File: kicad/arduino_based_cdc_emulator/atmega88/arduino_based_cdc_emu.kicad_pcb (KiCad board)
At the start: 2 copper layers, 13 parts, among them IC1 ATMEGA88-A, P1 CONN_5, P2 CONN_2, U1 78L05, X1 20MHz

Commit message: same changes
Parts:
- added P3: CONN_3, Pin_Headers:Pin_Header_Straight_1x01, F.Cu at (104.6, 107.1)
- P1: value CONN_5 -> CONN_1
- P2: footprint Pin_Headers:Pin_Header_Straight_1x02 -> Pin_Headers:Pin_Header_Straight_1x05
- moved P1 39.5 mm to (101.4, 117.1)
- moved C2 25.0 mm to (116.8, 107.0), turned to 180 degrees
- moved C1 24.1 mm to (101.9, 104.5), turned to 270 degrees
- moved X1 23.2 mm to (111.5, 103.2)
- moved C3 21.6 mm to (114.2, 119.6), turned to 90 degrees
- moved P2 17.5 mm to (124.1, 114.2), turned to 180 degrees
- moved IC1 15.6 mm to (109.5, 112.0)
- moved R4 14.1 mm to (121.5, 105.1), turned to 90 degrees
- moved R1 14.0 mm to (104.4, 119.3), turned to 90 degrees
- moved R3 13.4 mm to (119.3, 112.6), turned to 0 degrees
- moved C4 10.3 mm to (119.3, 114.9), turned to 180 degrees
- moved U1 9.58 mm to (120.8, 120.0), turned to 270 degrees
- moved R2 7.68 mm to (109.5, 120.5), turned to 180 degrees
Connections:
- IC1 pad 16: (no net) -> /MISO
- IC1 pad 19: Net-(C1-Pad2) -> (no net)
- IC1 pad 22: Net-(C2-Pad2) -> (no net)
- IC1 pad 29: Net-(IC1-Pad29) -> /RESET
- IC1 pad 7: (no net) -> Net-(C2-Pad2)
- IC1 pad 8: (no net) -> Net-(C1-Pad2)
- P2 pad 1: RX -> +5V
- P2 pad 2: TX -> /RESET
- R3 pad 1: Net-(IC1-Pad29) -> /RESET
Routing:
- net GND: track 46.7 -> 106.8 mm
- net /DataIn: track 34.0 -> 4.40 mm
- net +5V: track 65.6 -> 40.8 mm
- net /DataOut: track 12.7 -> 34.1 mm
- net /Clock: track 26.3 -> 7.78 mm
- net Net-(IC1-Pad15): track 3.04 -> 17.2 mm
- net /RESET: track 0.00 -> 11.9 mm
- net /MISO: track 0.00 -> 9.94 mm
- net +12V: track 10.8 -> 20.1 mm
- net Net-(IC1-Pad29): track 8.33 -> 0.00 mm
- net Net-(C2-Pad2): track 23.4 -> 17.5 mm
- net Net-(C1-Pad2): track 10.2 -> 14.8 mm
- net Net-(IC1-Pad32): track 5.63 -> 8.87 mm
- net RX: track 12.2 -> 10.5 mm
- net TX: track 12.7 -> 11.5 mm
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- removed copper zone on F.Cu, net GND
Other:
- board outline added: 26.6 x 23.5 mm

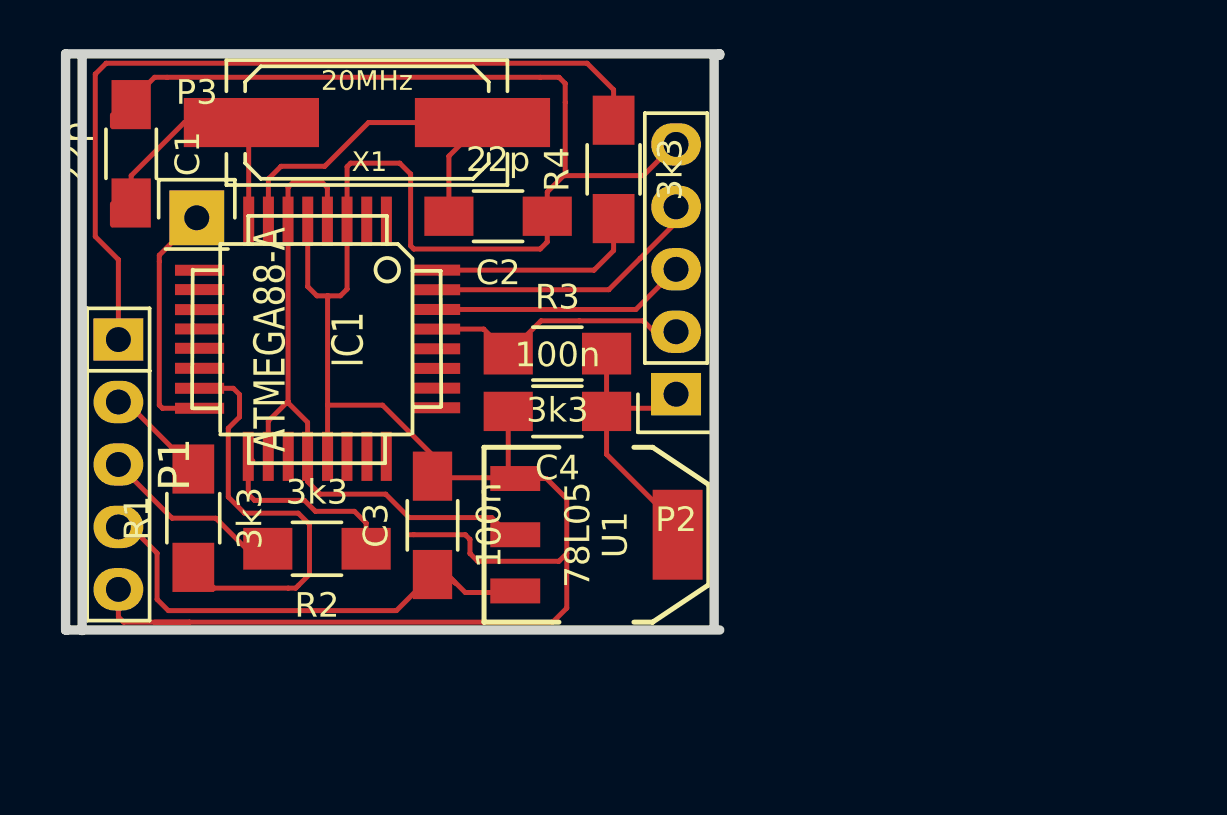
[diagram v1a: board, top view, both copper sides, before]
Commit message: pcb, really need rework.
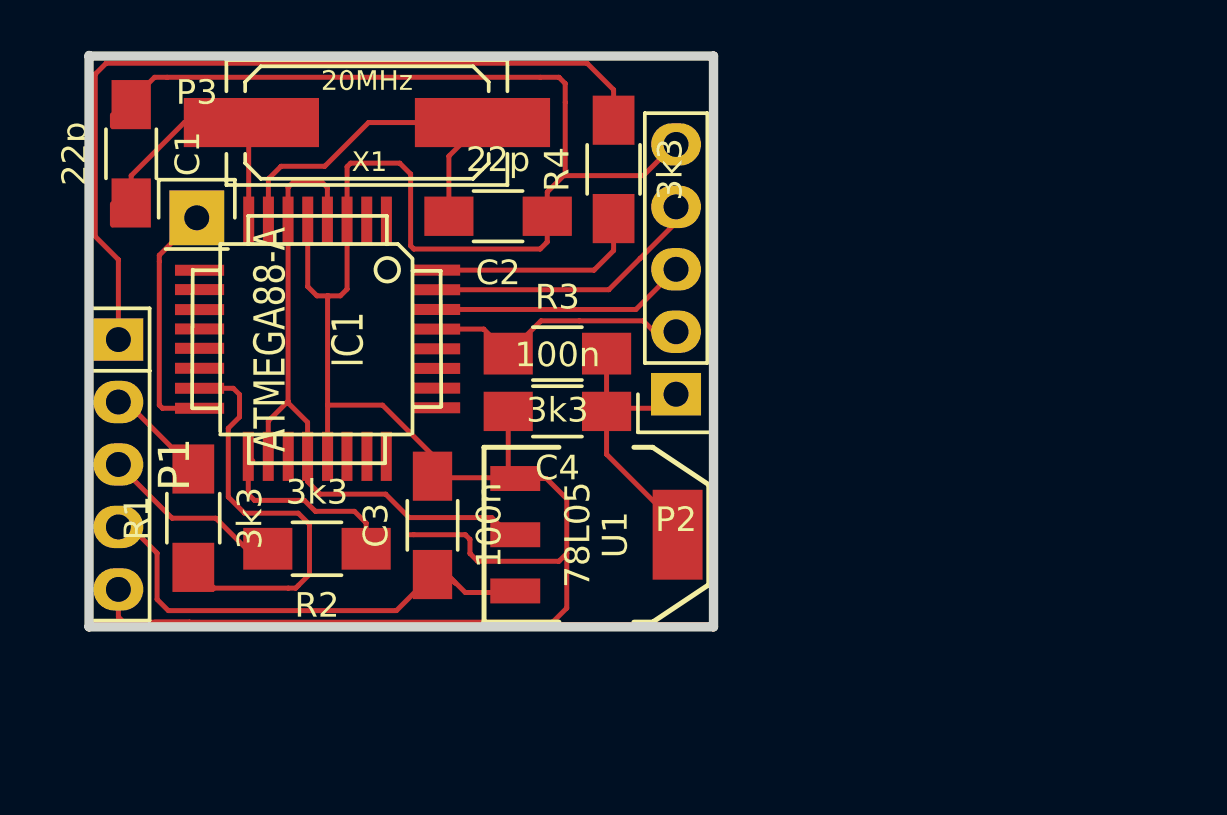
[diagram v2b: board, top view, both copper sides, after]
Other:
- board size 26.6 x 23.5 mm -> 25.4 x 23.2 mm
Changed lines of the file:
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@@
-(kicad_pcb (version 4) (host pcbnew 0.201505041002+5641~23~ubuntu14.04.1-product)
+(kicad_pcb (version 4) (host pcbnew 0.201511171411+6319~30~ubuntu14.04.1-product)
   (general
     (links 34)
     (no_connects 1)
-    (area 96.636115 92.566902 136.873055 124.333001)
+    (area 98.4385 95.5548 137.922002 124.015501)
     (thickness 1.6002)
-    (drawings 8)
+    (drawings 6)
     (tracks 187)
     (zones 0)
@@
     )
   )
-  (gr_line (start 125.6284 123.7996) (end 125.6284 100.4316) (angle 90) (layer Edge.Cuts) (width 0.381))
-  (gr_line (start 99.9236 100.4316) (end 99.9744 100.4316) (angle 90) (layer Edge.Cuts) (width 0.381))
-  (gr_line (start 99.9236 123.8504) (end 99.9236 100.4316) (angle 90) (layer Edge.Cuts) (width 0.381))
-  (gr_line (start 99.2505 123.825) (end 99.314 123.825) (angle 90) (layer Edge.Cuts) (width 0.381))
-  (gr_line (start 99.2505 100.3935) (end 99.2505 123.825) (angle 90) (layer Edge.Cuts) (width 0.381))
-  (gr_line (start 99.2505 123.825) (end 125.857 123.825) (angle 90) (layer Edge.Cuts) (width 0.381))
-  (gr_line (start 125.857 100.3935) (end 125.857 100.457) (angle 90) (layer Edge.Cuts) (width 0.381))
-  (gr_line (start 99.2505 100.3935) (end 125.857 100.3935) (angle 90) (layer Edge.Cuts) (width 0.381))
+  (gr_line (start 125.603 123.698) (end 125.603 100.4824) (angle 90) (layer Edge.Cuts) (width 0.381))
+  (gr_line (start 100.203 123.698) (end 125.603 123.698) (angle 90) (layer Edge.Cuts) (width 0.381))
+  (gr_line (start 100.203 100.4824) (end 125.603 100.4824) (angle 90) (layer Edge.Cuts) (width 0.381))
+  (dimension 25.4 (width 0.3048) (layer Dwgs.User)
+    (gr_text "25.400 mm" (at 112.903 97.4344) (layer Dwgs.User)
+      (effects (font (size 2.032 1.524) (thickness 0.3048)))
+    )
+    (feature1 (pts (xy 125.603 100.457) (xy 125.603 95.8088)))
+    (feature2 (pts (xy 100.203 100.457) (xy 100.203 95.8088)))
+    (crossbar (pts (xy 100.203 99.06) (xy 125.603 99.06)))
+    (arrow1a (pts (xy 125.603 99.06) (xy 124.476496 99.646421)))
+    (arrow1b (pts (xy 125.603 99.06) (xy 124.476496 98.473579)))
+    (arrow2a (pts (xy 100.203 99.06) (xy 101.329504 99.646421)))
+    (arrow2b (pts (xy 100.203 99.06) (xy 101.329504 98.473579)))
+  )
+  (gr_line (start 100.203 100.457) (end 100.203 123.698) (angle 90) (layer Edge.Cuts) (width 0.381))
+  (dimension 23.495 (width 0.3048) (layer Dwgs.User)
+    (gr_text "23.495 mm" (at 131.1656 112.0775 270) (layer Dwgs.User)
+      (effects (font (size 2.032 1.524) (thickness 0.3048)))
+    )
+    (feature1 (pts (xy 125.603 123.825) (xy 132.7912 123.825)))
+    (feature2 (pts (xy 125.603 100.33) (xy 132.7912 100.33)))
+    (crossbar (pts (xy 129.54 100.33) (xy 129.54 123.825)))
+    (arrow1a (pts (xy 129.54 123.825) (xy 128.953579 122.698496)))
+    (arrow1b (pts (xy 129.54 123.825) (xy 130.126421 122.698496)))
+    (arrow2a (pts (xy 129.54 100.33) (xy 128.953579 101.456504)))
+    (arrow2b (pts (xy 129.54 100.33) (xy 130.126421 101.456504)))
+  )
   (segment (start 108.29798 107.19816) (end 108.29798 105.82402) (width 0.2032) (layer Front) (net 1))
   (segment (start 109.6645 105.6005) (end 109.89818 105.83418) (width 0.2032) (layer Front) (net 1))
@@
   (segment (start 123.444 118.872) (end 124.206 119.634) (width 0.2032) (layer Front) (net 1))
   (segment (start 121.253 116.681) (end 124.206 119.634) (width 0.2032) (layer Front) (net 1))
-  (segment (start 107.474 120.523) (end 106.6038 120.523) (width 0.2032) (layer Front) (net 2) (status C00000))
-  (segment (start 106.6038 120.523) (end 105.3592 119.2784) (width 0.2032) (layer Front) (net 2) (status 400000))
+  (segment (start 107.474 120.523) (end 106.6038 120.523) (width 0.2032) (layer Front) (net 2))
+  (segment (start 106.6038 120.523) (end 105.3592 119.2784) (width 0.2032) (layer Front) (net 2))
   (segment (start 105.3592 119.2784) (end 103.5812 119.2784) (width 0.2032) (layer Front) (net 2))
-  (segment (start 103.5812 119.2784) (end 101.3968 117.094) (width 0.2032) (layer Front) (net 2) (status 800000))
+  (segment (start 103.5812 119.2784) (end 101.3968 117.094) (width 0.2032) (layer Front) (net 2))
   (segment (start 106.712 120.8405) (end 106.712 120.555) (width 0.2032) (layer Front) (net 2))
-  (segment (start 101.3968 114.554) (end 101.7204 114.554) (width 0.2032) (layer Front) (net 3) (status C00000))
-  (segment (start 101.7204 114.554) (end 104.4448 117.2784) (width 0.2032) (layer Front) (net 3) (status C00000))
+  (segment (start 101.3968 114.554) (end 101.7204 114.554) (width 0.2032) (layer Front) (net 3))
+  (segment (start 101.7204 114.554) (end 104.4448 117.2784) (width 0.2032) (layer Front) (net 3))
   (segment (start 103.9495 116.8085) (end 103.9495 116.586) (width 0.2032) (layer Front) (net 3))
-  (segment (start 101.3968 112.014) (end 101.3968 108.7628) (width 0.2032) (layer Front) (net 4) (status 400000))
+  (segment (start 101.3968 112.014) (end 101.3968 108.7628) (width 0.2032) (layer Front) (net 4))
   (segment (start 101.3968 108.7628) (end 100.457 107.823) (width 0.2032) (layer Front) (net 4))
   (segment (start 100.457 101.219) (end 100.9015 100.7745) (width 0.2032) (layer Front) (net 4))
@@
   (segment (start 120.4595 100.7745) (end 100.9015 100.7745) (width 0.2032) (layer Front) (net 4))
   (segment (start 104.2924 123.5075) (end 101.6127 123.5075) (width 0.2032) (layer Front) (net 5))
-  (segment (start 101.3968 123.2916) (end 101.3968 122.174) (width 0.2032) (layer Front) (net 5) (status 800000))
+  (segment (start 101.3968 123.2916) (end 101.3968 122.174) (width 0.2032) (layer Front) (net 5))
   (segment (start 101.6127 123.5075) (end 101.3968 123.2916) (width 0.2032) (layer Front) (net 5))
   (segment (start 101.9175 102.4575) (end 101.9175 102.2985) (width 0.2032) (layer Front) (net 5))
@@
   (segment (start 113.697 103.156) (end 113.665 103.124) (width 0.2032) (layer Front) (net 7))
   (segment (start 115.602 103.664) (end 115.062 103.124) (width 0.2032) (layer Front) (net 7))
-  (segment (start 101.3968 119.634) (end 101.9048 119.634) (width 0.2032) (layer Front) (net 8) (status C00000))
-  (segment (start 101.9048 119.634) (end 102.9716 120.7008) (width 0.2032) (layer Front) (net 8) (status 400000))
+  (segment (start 101.3968 119.634) (end 101.9048 119.634) (width 0.2032) (layer Front) (net 8))
+  (segment (start 101.9048 119.634) (end 102.9716 120.7008) (width 0.2032) (layer Front) (net 8))
   (segment (start 102.9716 120.7008) (end 102.9716 122.5804) (width 0.2032) (layer Front) (net 8))
   (segment (start 102.9716 122.5804) (end 103.4288 123.0376) (width 0.2032) (layer Front) (net 8))
   (segment (start 103.4288 123.0376) (end 112.7059 123.0376) (width 0.2032) (layer Front) (net 8))
-  (segment (start 112.7059 123.0376) (end 114.173 121.5705) (width 0.2032) (layer Front) (net 8) (status 800000))
+  (segment (start 112.7059 123.0376) (end 114.173 121.5705) (width 0.2032) (layer Front) (net 8))
   (segment (start 114.808 121.634) (end 114.8395 121.634) (width 0.2032) (layer Front) (net 8))
   (segment (start 114.8395 121.634) (end 115.5065 122.301) (width 0.2032) (layer Front) (net 8))

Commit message: updates
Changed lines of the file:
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@@
-(kicad_pcb (version 4) (host pcbnew 0.201511171411+6319~30~ubuntu14.04.1-product)
+(kicad_pcb (version 20160815) (host pcbnew 4.1.0-alpha+201608211231+7083~46~ubuntu16.04.1-product)
   (general
     (links 34)
     (no_connects 1)
-    (area 98.4385 95.5548 137.922002 124.015501)
+    (area 99.797799 95.8088 137.922001 123.88946)
     (thickness 1.6002)
     (drawings 6)
@@
     (pad_to_mask_clearance 0.254)
     (aux_axis_origin 0 0)
-    (visible_elements FFFFFF7F)
+    (visible_elements FFFEFF7F)
     (pcbplotparams
       (layerselection 0x00030_80000001)
@@
       (hpglpenspeed 20)
       (hpglpendiameter 15)
-      (hpglpenoverlay 2)
       (psnegative false)
       (psa4output false)
@@
     (uvia_dia 0.508)
     (uvia_drill 0.127)
+    (diff_pair_gap 0.25)
+    (diff_pair_width 0.2)
     (add_net +12V)
     (add_net +5V)
@@
     (tags "capacitor 1206")
     (attr smd)
-    (fp_text reference C1 (at 0 -2.3 270) (layer F.SilkS)
-      (effects (font (size 1 1) (thickness 0.15)))
-    )
-    (fp_text value 22p (at 0 2.3 270) (layer F.SilkS)
+    (fp_text reference C1 (at 4.3925 -0.1325 270) (layer F.SilkS)
+      (effects (font (size 1 1) (thickness 0.15)))
+    )
+    (fp_text value 22p (at 4.7371 0.0508 270) (layer F.SilkS)
       (effects (font (size 1 1) (thickness 0.15)))
     )
@@
       (effects (font (size 1 1) (thickness 0.15)))
     )
-    (fp_text value 22p (at 0 2.3 180) (layer F.SilkS)
+    (fp_text value 22p (at -2.6543 -1.8034 180) (layer F.SilkS)
       (effects (font (size 1 1) (thickness 0.15)))
     )
@@
     (tags "capacitor 1206")
     (attr smd)
-    (fp_text reference C3 (at 0 -2.3 90) (layer F.SilkS)
-      (effects (font (size 1 1) (thickness 0.15)))
-    )
-    (fp_text value 100n (at 0 2.3 90) (layer F.SilkS)
+    (fp_text reference C3 (at 0.8205 -2.123 180) (layer F.SilkS)
+      (effects (font (size 1 1) (thickness 0.15)))
+    )
+    (fp_text value 100n (at 1.57734 1.55448 90) (layer F.SilkS)
       (effects (font (size 1 1) (thickness 0.15)))
     )
@@
     (tags "capacitor 1206")
     (attr smd)
-    (fp_text reference C4 (at 0 -2.3 180) (layer F.SilkS)
-      (effects (font (size 1 1) (thickness 0.15)))
-    )
-    (fp_text value 100n (at 0 2.3 180) (layer F.SilkS)
+    (fp_text reference C4 (at 0.003 4.185 360) (layer F.SilkS)
+      (effects (font (size 1 1) (thickness 0.15)))
+    )
+    (fp_text value 100n (at -1.47828 4.40436 180) (layer F.SilkS)
       (effects (font (size 1 1) (thickness 0.15)))
     )
@@
   (module SMD_Packages:TQFP-32 (layer Front)
     (at 109.474 112.014 270)
-    (fp_text reference IC1 (at 0 -1.27 270) (layer F.SilkS)
+    (fp_text reference IC1 (at 0.036 -2.126 270) (layer F.SilkS)
       (effects (font (size 1.27 1.016) (thickness 0.2032)))
     )
@@
     (descr "Through hole pin header")
     (tags "pin header")
-    (fp_text reference P1 (at 0 -2.286 270) (layer F.SilkS)
+    (fp_text reference P1 (at 0 -2.286 270) (layer F.SilkS) hide
       (effects (font (size 1.27 1.27) (thickness 0.2032)))
     )
@@
     (tags "resistor 1206")
     (attr smd)
-    (fp_text reference R1 (at 0 -2.3 90) (layer F.SilkS)
-      (effects (font (size 1 1) (thickness 0.15)))
-    )
-    (fp_text value 3k3 (at 0 2.3 90) (layer F.SilkS)
+    (fp_text reference R1 (at 0.55118 2.15646) (layer F.SilkS)
+      (effects (font (size 1 1) (thickness 0.15)))
+    )
+    (fp_text value 3k3 (at 0.47752 2.65176 180) (layer F.SilkS)
       (effects (font (size 1 1) (thickness 0.15)))
     )
@@
     (tags "resistor 1206")
     (attr smd)
-    (fp_text reference R2 (at 0 -2.3 180) (layer F.SilkS)
-      (effects (font (size 1 1) (thickness 0.15)))
-    )
-    (fp_text value 3k3 (at 0 2.3 180) (layer F.SilkS)
+    (fp_text reference R2 (at 0.0508 -2.11328 180) (layer F.SilkS)
+      (effects (font (size 1 1) (thickness 0.15)))
+    )
+    (fp_text value 3k3 (at 1.40208 -2.21996 180) (layer F.SilkS)
       (effects (font (size 1 1) (thickness 0.15)))
     )
@@
     (tags "resistor 1206")
     (attr smd)
-    (fp_text reference R3 (at 0 -2.3) (layer F.SilkS)
-      (effects (font (size 1 1) (thickness 0.15)))
-    )
-    (fp_text value 3k3 (at 0 2.3) (layer F.SilkS)
+    (fp_text reference R3 (at -0.053 -3.2855) (layer F.SilkS)
+      (effects (font (size 1 1) (thickness 0.15)))
+    )
+    (fp_text value 3k3 (at 3.06832 4.68122) (layer F.SilkS)
       (effects (font (size 1 1) (thickness 0.15)))
     )
@@
     (tags "resistor 1206")
     (attr smd)
-    (fp_text reference R4 (at 0 -2.3 90) (layer F.SilkS)
-      (effects (font (size 1 1) (thickness 0.15)))
-    )
-    (fp_text value 3k3 (at 0 2.3 90) (layer F.SilkS)
+    (fp_text reference R4 (at 2.1425 -1.689 90) (layer F.SilkS)
+      (effects (font (size 1 1) (thickness 0.15)))
+    )
+    (fp_text value 3k3 (at 3.4163 2.54 180) (layer F.SilkS)
       (effects (font (size 1 1) (thickness 0.15)))
     )
@@
   (module Crystals_Oscillators_SMD:Q_49U3HMS (layer Front)
     (at 111.506 103.1875 180)
-    (fp_text reference X1 (at -0.1 -1.6 180) (layer F.SilkS)
+    (fp_text reference X1 (at 6.856 1.8875 180) (layer F.SilkS)
       (effects (font (size 0.8 0.8) (thickness 0.15)))
     )
@@
     (descr "Through hole pin header")
     (tags "pin header")
-    (fp_text reference P2 (at 0 -5.1 180) (layer F.SilkS)
+    (fp_text reference P2 (at 0 -5.1 180) (layer F.SilkS) hide
       (effects (font (size 1 1) (thickness 0.15)))
     )
@@
     (descr "Through hole pin header")
     (tags "pin header")
-    (fp_text reference P3 (at 0 -5.1) (layer F.SilkS)
+    (fp_text reference P3 (at 0 -5.1) (layer F.SilkS) hide
       (effects (font (size 1 1) (thickness 0.15)))
     )
@@
   (segment (start 123.444 118.872) (end 124.206 119.634) (width 0.2032) (layer Front) (net 1))
   (segment (start 121.253 116.681) (end 124.206 119.634) (width 0.2032) (layer Front) (net 1))
-  (segment (start 107.474 120.523) (end 106.6038 120.523) (width 0.2032) (layer Front) (net 2))
-  (segment (start 106.6038 120.523) (end 105.3592 119.2784) (width 0.2032) (layer Front) (net 2))
+  (segment (start 107.474 120.523) (end 106.6038 120.523) (width 0.2032) (layer Front) (net 2) (status 30))
+  (segment (start 106.6038 120.523) (end 105.3592 119.2784) (width 0.2032) (layer Front) (net 2) (status 10))
   (segment (start 105.3592 119.2784) (end 103.5812 119.2784) (width 0.2032) (layer Front) (net 2))
   (segment (start 103.5812 119.2784) (end 101.3968 117.094) (width 0.2032) (layer Front) (net 2))
-  (segment (start 106.712 120.8405) (end 106.712 120.555) (width 0.2032) (layer Front) (net 2))
+  (segment (start 106.712 120.8405) (end 106.712 120.555) (width 0.2032) (layer Front) (net 2) (status 30))
   (segment (start 101.3968 114.554) (end 101.7204 114.554) (width 0.2032) (layer Front) (net 3))
   (segment (start 101.7204 114.554) (end 104.4448 117.2784) (width 0.2032) (layer Front) (net 3))
@@
   (segment (start 114.808 121.634) (end 114.808 122.428) (width 0.2032) (layer Front) (net 8))
   (segment (start 115.094 121.92) (end 114.808 121.634) (width 0.2032) (layer Front) (net 8))
-  (segment (start 111.474 120.523) (end 111.474 119.475) (width 0.2032) (layer Front) (net 9))
+  (segment (start 111.474 120.523) (end 111.474 119.475) (width 0.2032) (layer Front) (net 9) (status 10))
   (segment (start 110.998 118.999) (end 109.4105 118.999) (width 0.2032) (layer Front) (net 9))
   (segment (start 111.474 119.475) (end 110.998 118.999) (width 0.2032) (layer Front) (net 9))
@@
   (segment (start 106.934 118.5545) (end 108.966 118.5545) (width 0.2032) (layer Front) (net 9))
   (segment (start 106.68 118.3005) (end 106.934 118.5545) (width 0.2032) (layer Front) (net 9))
-  (segment (start 111.347 120.4595) (end 110.8075 120.4595) (width 0.2032) (layer Front) (net 9))
+  (segment (start 111.347 120.4595) (end 110.8075 120.4595) (width 0.2032) (layer Front) (net 9) (status 30))
   (segment (start 106.8705 116.9543) (end 106.68 116.7638) (width 0.2032) (layer Front) (net 9))
-  (segment (start 111.347 120.4595) (end 111.1885 120.4595) (width 0.2032) (layer Front) (net 9))
+  (segment (start 111.347 120.4595) (end 111.1885 120.4595) (width 0.2032) (layer Front) (net 9) (status 30))
   (segment (start 114.3 109.18952) (end 120.74398 109.18952) (width 0.2032) (layer Front) (net 10))
   (segment (start 121.539 108.3945) (end 121.539 107.0925) (width 0.2032) (layer Front) (net 10))
